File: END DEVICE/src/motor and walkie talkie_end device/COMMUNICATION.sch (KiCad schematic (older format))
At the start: 20 parts, among them IC1 LM4871, J3 speaker_conn, U2 Ai-Thinker-Ra-02, U3 SA818-1W, U4 LP_Filter, U5 MCP41010

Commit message: third commit:very minor changes
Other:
- moved on the sheet: C9, U2
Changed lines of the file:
@@
 Wire Wire Line
 	8300 2050 8300 1850
-Text GLabel 2000 6150 0    50   Input ~ 0
+Text GLabel 3800 6150 0    50   Input ~ 0
 MOSI
-Text GLabel 2000 6050 0    50   Input ~ 0
+Text GLabel 3800 6050 0    50   Input ~ 0
 MISO
-Text GLabel 2000 5950 0    50   Input ~ 0
+Text GLabel 3800 5950 0    50   Input ~ 0
 SCK
 $Comp
 L power:+3.3V #PWR0136
 U 1 1 614532C2
-P 2700 4950
-F 0 "#PWR0136" H 2700 4800 50  0001 C CNN
-F 1 "+3.3V" H 2715 5123 50  0000 C CNN
-F 2 "" H 2700 4950 50  0001 C CNN
-F 3 "" H 2700 4950 50  0001 C CNN
-	1    2700 4950
+P 4500 4950
+F 0 "#PWR0136" H 4500 4800 50  0001 C CNN
+F 1 "+3.3V" H 4515 5123 50  0000 C CNN
+F 2 "" H 4500 4950 50  0001 C CNN
+F 3 "" H 4500 4950 50  0001 C CNN
+	1    4500 4950
 	1    0    0    -1
 $EndComp
 Wire Wire Line
-	2200 6150 2000 6150
+	4000 6150 3800 6150
 Wire Wire Line
-	2000 6050 2200 6050
+	3800 6050 4000 6050
 Wire Wire Line
-	2200 5950 2000 5950
+	4000 5950 3800 5950
 Wire Wire Line
-	2000 5850 2200 5850
+	3800 5850 4000 5850
 Wire Wire Line
-	2200 5650 2000 5650
+	4000 5650 3800 5650
 $Comp
 L Device:C_Small C?
 U 1 1 614532CD
-P 3600 5050
+P 5400 5050
 AR Path="/614532CD" Ref="C?"  Part="1"
 AR Path="/6131B829/614532CD" Ref="C9"  Part="1"
-F 0 "C9" V 3829 5050 50  0000 C CNN
-F 1 "100nF" V 3738 5050 50  0000 C CNN
-F 2 "" H 3600 5050 50  0001 C CNN
-F 3 "~" H 3600 5050 50  0001 C CNN
-	1    3600 5050
+F 0 "C9" V 5629 5050 50  0000 C CNN
+F 1 "100nF" V 5538 5050 50  0000 C CNN
+F 2 "" H 5400 5050 50  0001 C CNN
+F 3 "~" H 5400 5050 50  0001 C CNN
+	1    5400 5050
 	-1   0    0    1
 $EndComp
@@
 L remote_devices:Ai-Thinker-Ra-02 U?
 U 1 1 614532D3
-P 2700 5950
+P 4500 5950
 AR Path="/614532D3" Ref="U?"  Part="1"
 AR Path="/6131B829/614532D3" Ref="U2"  Part="1"
-F 0 "U2" H 2250 6700 50  0000 C CNN
-F 1 "Ai-Thinker-Ra-02" H 2250 6600 50  0000 C CNN
-F 2 "Remote_devices:Ai-Thinker-Ra-02-LoRa" H 3700 5550 50  0001 C CNN
-F 3 "https://mikroelectron.com/Product/10KM-433M-LORA-LONG-RANGE-WIRELESS-MODULE-RA-01" H 2800 6650 50  0001 C CNN
-	1    2700 5950
+F 0 "U2" H 4050 6700 50  0000 C CNN
+F 1 "Ai-Thinker-Ra-02" H 4050 6600 50  0000 C CNN
+F 2 "Remote_devices:Ai-Thinker-Ra-02-LoRa" H 5500 5550 50  0001 C CNN
+F 3 "https://mikroelectron.com/Product/10KM-433M-LORA-LONG-RANGE-WIRELESS-MODULE-RA-01" H 4600 6650 50  0001 C CNN
+	1    4500 5950
 	1    0    0    -1
 $EndComp
 Wire Wire Line
-	3600 4900 3600 4950
+	5400 4900 5400 4950
 $Comp
 L power:GND #PWR0137
 U 1 1 614532DA
-P 3600 5200
-F 0 "#PWR0137" H 3600 4950 50  0001 C CNN
-F 1 "GND" H 3605 5027 50  0000 C CNN
-F 2 "" H 3600 5200 50  0001 C CNN
-F 3 "" H 3600 5200 50  0001 C CNN
-	1    3600 5200
+P 5400 5200
+F 0 "#PWR0137" H 5400 4950 50  0001 C CNN
+F 1 "GND" H 5405 5027 50  0000 C CNN
+F 2 "" H 5400 5200 50  0001 C CNN
+F 3 "" H 5400 5200 50  0001 C CNN
+	1    5400 5200
 	1    0    0    -1
 $EndComp
@@
 L power:GND #PWR0138
 U 1 1 614532E0
-P 2700 6800
-F 0 "#PWR0138" H 2700 6550 50  0001 C CNN
-F 1 "GND" H 2705 6627 50  0000 C CNN
-F 2 "" H 2700 6800 50  0001 C CNN
-F 3 "" H 2700 6800 50  0001 C CNN
-	1    2700 6800
+P 4500 6800
+F 0 "#PWR0138" H 4500 6550 50  0001 C CNN
+F 1 "GND" H 4505 6627 50  0000 C CNN
+F 2 "" H 4500 6800 50  0001 C CNN
+F 3 "" H 4500 6800 50  0001 C CNN
+	1    4500 6800
 	1    0    0    -1
 $EndComp
 Wire Wire Line
-	2700 6800 2700 6750
+	4500 6800 4500 6750
 Wire Wire Line
-	2600 6650 2600 6750
+	4400 6650 4400 6750
 Wire Wire Line
-	2600 6750 2700 6750
+	4400 6750 4500 6750
 Wire Wire Line
-	2800 6650 2800 6750
+	4600 6650 4600 6750
 Wire Wire Line
-	2800 6750 2700 6750
-Connection ~ 2700 6750
-Text GLabel 3400 5550 2    50   Input ~ 0
+	4600 6750 4500 6750
+Connection ~ 4500 6750
+Text GLabel 5200 5550 2    50   Input ~ 0
 DIO0
 Wire Wire Line
-	2700 4950 2700 5050
+	4500 4950 4500 5050
 Wire Wire Line
-	3600 5200 3600 5150
+	5400 5200 5400 5150
 Wire Wire Line
-	3600 4900 3100 4900
+	5400 4900 4900 4900
 Wire Wire Line
-	3100 4900 3100 5050
+	4900 4900 4900 5050
 Wire Wire Line
-	3100 5050 2700 5050
-Connection ~ 2700 5050
+	4900 5050 4500 5050
+Connection ~ 4500 5050
 Wire Wire Line
-	2700 5050 2700 5150
-Text GLabel 3400 5650 2    50   Input ~ 0
+	4500 5050 4500 5150
+Text GLabel 5200 5650 2    50   Input ~ 0
 DIO1
-Text GLabel 3400 5750 2    50   Input ~ 0
+Text GLabel 5200 5750 2    50   Input ~ 0
 DIO2
 Wire Wire Line
-	3200 5550 3400 5550
+	5000 5550 5200 5550
 Wire Wire Line
-	3400 5650 3200 5650
+	5200 5650 5000 5650
 Wire Wire Line
-	3200 5750 3400 5750
-NoConn ~ 3200 5850
-NoConn ~ 3200 5950
-NoConn ~ 3200 6050
-Text Notes 1050 4650 0    50   ~ 10
+	5000 5750 5200 5750
+NoConn ~ 5000 5850
+NoConn ~ 5000 5950
+NoConn ~ 5000 6050
+Text Notes 2850 4650 0    50   ~ 10
 RA-02 LORA MODULE
 Wire Notes Line
-	4700 4400 4700 7700
+	6500 4400 6500 7700
 Wire Notes Line
-	4700 7700 600  7700
+	6500 7700 2400 7700
 Wire Notes Line
-	600  7700 600  4400
+	2400 7700 2400 4400
 Wire Notes Line
 	10850 2500 10850 2750
@@
 Text Notes 6150 3300 0    50   ~ 0
 Digital Potentiometer uses \nSPI protocol to change resistance\nused for setting the volume of the speaker
-Text GLabel 2000 5850 0    50   Input ~ 0
+Text GLabel 3800 5850 0    50   Input ~ 0
 lora_SS
 Text GLabel 5600 2300 0    50   Input ~ 0
@@
 Wire Notes Line
 	1150 2650 1200 2650
-Text GLabel 2000 5650 0    50   Input ~ 0
+Text GLabel 3800 5650 0    50   Input ~ 0
 RST
 Wire Notes Line
-	600  4400 4700 4400
+	2400 4400 6500 4400
 Wire Notes Line
 	4700 4250 600  4250

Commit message: commit 4:minor changes
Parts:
- U: renamed from U2; footprint Remote_devices:Ai-Thinker-Ra-02-LoRa -> RF_Module:Ai-Thinker-Ra-01-LoRa
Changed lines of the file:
@@
 P 4500 5950
 AR Path="/614532D3" Ref="U?"  Part="1"
-AR Path="/6131B829/614532D3" Ref="U2"  Part="1"
-F 0 "U2" H 4050 6700 50  0000 C CNN
+AR Path="/6131B829/614532D3" Ref="U"  Part="1"
+F 0 "U" H 4050 6700 50  0000 C CNN
 F 1 "Ai-Thinker-Ra-02" H 4050 6600 50  0000 C CNN
-F 2 "Remote_devices:Ai-Thinker-Ra-02-LoRa" H 5500 5550 50  0001 C CNN
+F 2 "RF_Module:Ai-Thinker-Ra-01-LoRa" H 5500 5550 50  0001 C CNN
 F 3 "https://mikroelectron.com/Product/10KM-433M-LORA-LONG-RANGE-WIRELESS-MODULE-RA-01" H 4600 6650 50  0001 C CNN
 	1    4500 5950
@@
 Wire Wire Line
 	5400 4900 5400 4950
-$Comp
-L power:GND #PWR0137
-U 1 1 614532DA
-P 5400 5200
-F 0 "#PWR0137" H 5400 4950 50  0001 C CNN
-F 1 "GND" H 5405 5027 50  0000 C CNN
-F 2 "" H 5400 5200 50  0001 C CNN
-F 3 "" H 5400 5200 50  0001 C CNN
-	1    5400 5200
-	1    0    0    -1
-$EndComp
 $Comp
 L power:GND #PWR0138
@@
 Wire Wire Line
 	4500 6800 4500 6750
-Wire Wire Line
-	4400 6650 4400 6750
 Wire Wire Line
 	4400 6750 4500 6750
@@
 Wire Notes Line
 	4700 4250 600  4250
+$Comp
+L power:GND #PWR0137
+U 1 1 62395891
+P 5400 5200
+F 0 "#PWR0137" H 5400 4950 50  0001 C CNN
+F 1 "GND" H 5405 5027 50  0000 C CNN
+F 2 "" H 5400 5200 50  0001 C CNN
+F 3 "" H 5400 5200 50  0001 C CNN
+	1    5400 5200
+	1    0    0    -1
+$EndComp
+Wire Wire Line
+	4400 6650 4400 6750
 $EndSCHEMATC

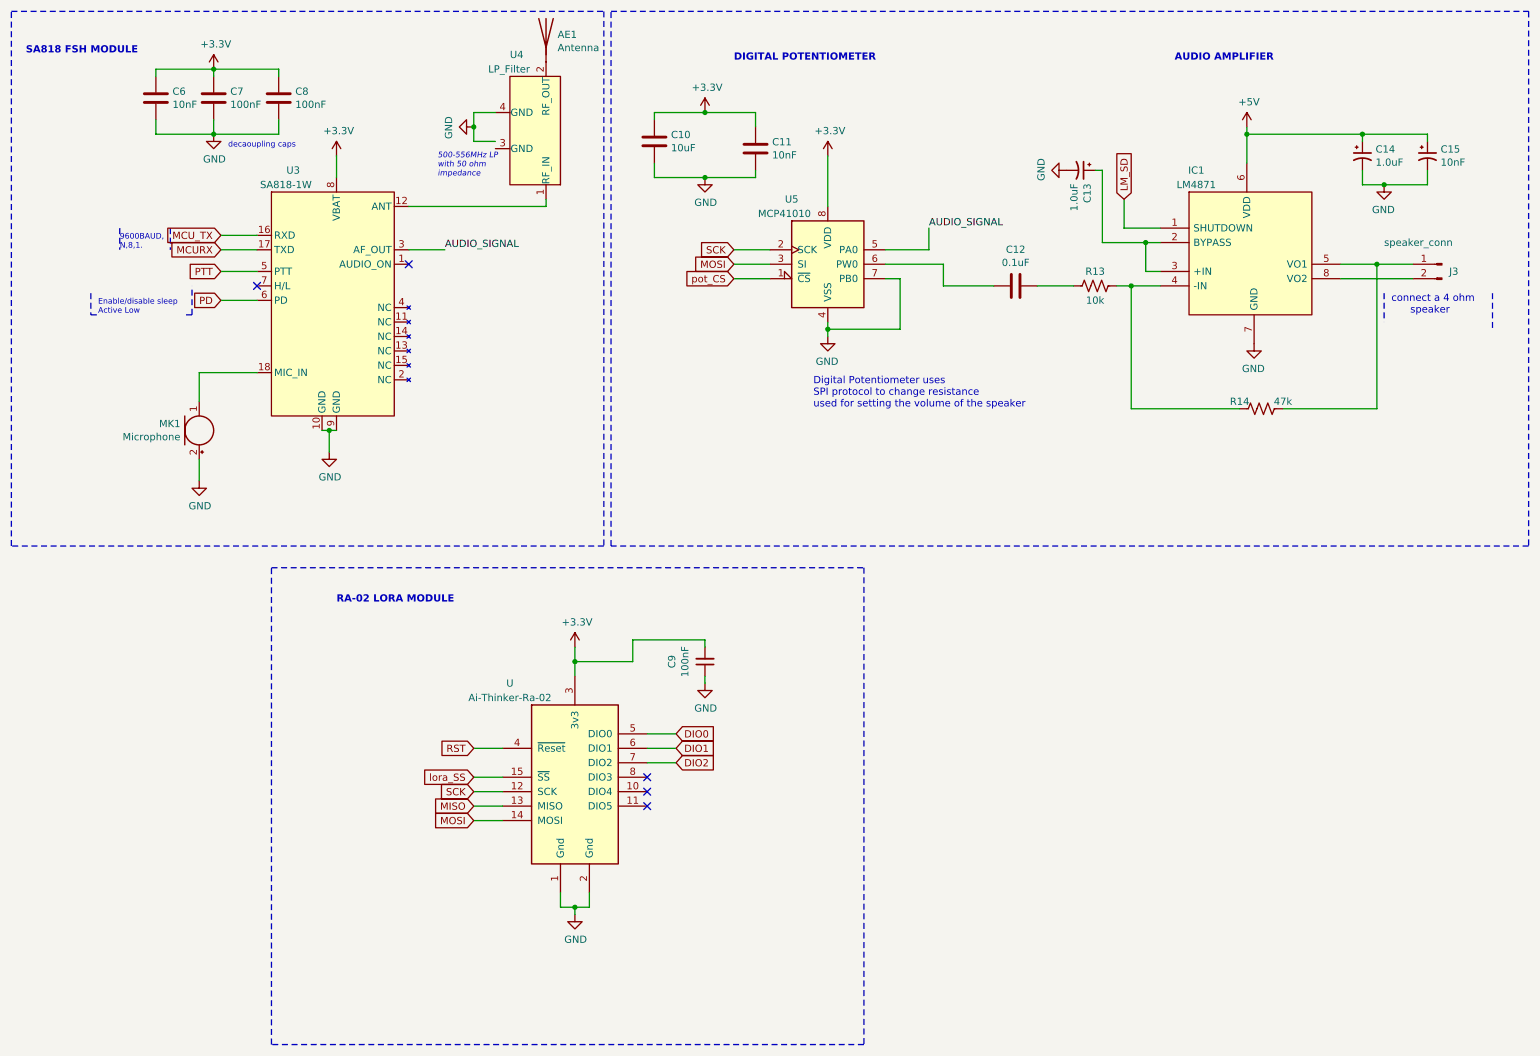
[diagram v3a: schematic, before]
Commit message: All footprint associations updated
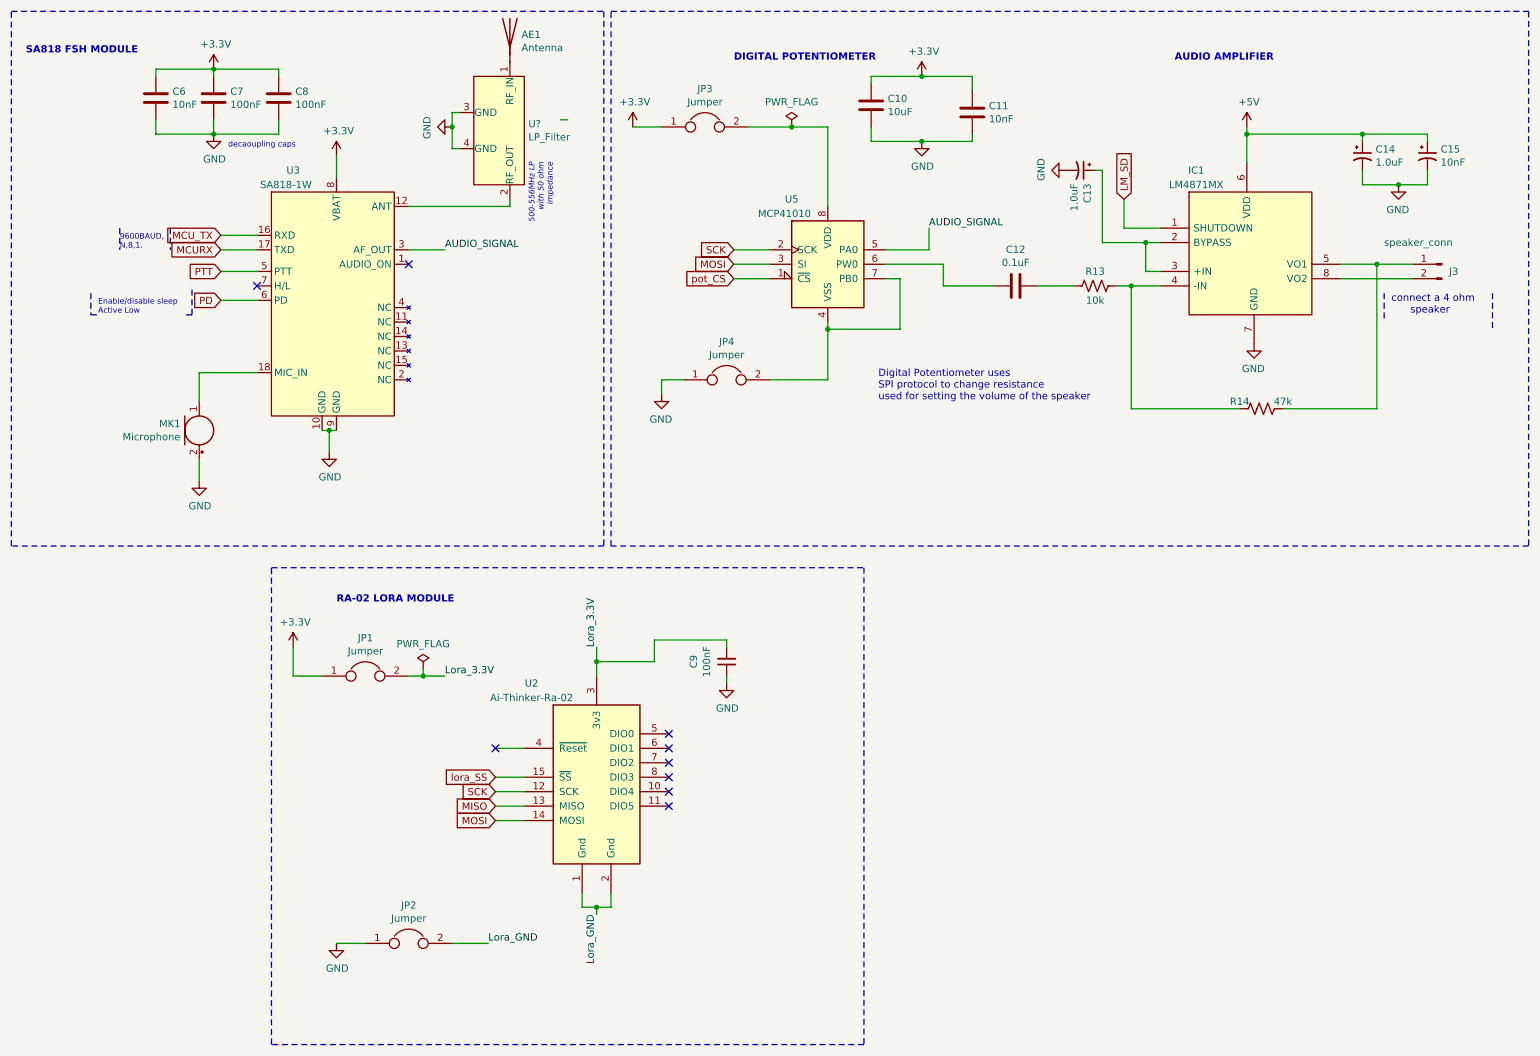
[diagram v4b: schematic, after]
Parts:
- removed U4: LP_Filter, symbol remote_devices:LP_Filter
- added JP1, JP2, JP3, JP4: Jumper, TestPoint:TestPoint_2Pads_Pitch2.54mm_Drill0.8mm, symbol Device:Jumper
- added U?: LP_Filter, symbol remote_devices:LP_Filter
- AE1: footprint (none) -> CoAxial connector:SMA_Amphenol_901-144_Vertical
- C10, C11, C12, C6, C7, C8, C9: footprint (none) -> Capacitor_SMD:C_0603_1608Metric
- C13, C14, C15: footprint (none) -> Capacitor_Tantalum_SMD:CP_EIA-2012-12_Kemet-R
- IC1: value LM4871 -> LM4871MX; footprint SOP65P490X110-8N -> Package_SO:SOP-8_3.9x4.9mm_P1.27mm
- J3: footprint (none) -> Connector_JST:JST_PH_B2B-PH-K_1x02_P2.00mm_Vertical
- MK1: footprint (none) -> Remote_devices:CMEJ974537P
- R13, R14: footprint (none) -> Resistor_SMD:R_0603_1608Metric
- U3: footprint (none) -> Remote_devices:SA818-1W
- U5: footprint (none) -> SamacSys_Parts_2:SOIC127P600X175-8N
- renumbered U to U2
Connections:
- net +3V3: now also JP1.1, JP3.1; no longer C9.2, U2.3 (3v3), U5.8 (VDD)
- net GND: now also JP2.1, JP4.1, U?.3 (GND), U?.4 (GND); no longer U2.1 (Gnd), U2.16 (Gnd), U2.2 (Gnd), U2.9 (Gnd), U5.4 (VSS), U5.7 (PB0)
- net at U3.12 (ANT): now also U?.2 (RF_OUT)
- net at AE1.1 (A): now also U?.1 (RF_IN)
- net DIO0: no longer names the net of U2.5 (DIO0)
- net DIO1: no longer names the net of U2.6 (DIO1)
- net DIO2: no longer names the net of U2.7 (DIO2)
- net RST: no longer names the net of U2.4 (~Reset)
- new net: JP4.2, U5.4 (VSS), U5.7 (PB0)
- new net: JP3.2, U5.8 (VDD)
- new net Lora_3.3V: C9.2, JP1.2, U2.3 (3v3)
- new net Lora_GND: JP2.2, U2.1 (Gnd), U2.16 (Gnd), U2.2 (Gnd), U2.9 (Gnd)
- no-connect marks 5 -> 9
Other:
- moved on the sheet: AE1, C10, C11, C9, U2

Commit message: Project 99% complete and ready:Revision Needed
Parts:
- U4: renamed from U?; footprint (none) -> Remote_devices:LFCN-530
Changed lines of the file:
@@
 	4050 1900 3350 1900
 $Comp
-L remote_devices:LP_Filter U?
+L remote_devices:LP_Filter U4
 U 1 1 627B3A36
 P 4150 1400
-F 0 "U?" V 4079 1428 50  0000 L CNN
+F 0 "U4" V 4079 1428 50  0000 L CNN
 F 1 "LP_Filter" V 4170 1428 50  0000 L CNN
-F 2 "" H 4150 1400 50  0001 C CNN
+F 2 "Remote_devices:LFCN-530" H 4150 1400 50  0001 C CNN
 F 3 "" H 4150 1400 50  0001 C CNN
 	1    4150 1400

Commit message: 90% complete and. PCB done with tracks and design rules verified as well as dimensions
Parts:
- removed C11: 10nF, Capacitor_SMD:C_0603_1608Metric, symbol Device:C
- removed JP3, JP4: Jumper, TestPoint:TestPoint_2Pads_Pitch2.54mm_Drill0.8mm, symbol Device:Jumper
- C14: value 1.0uF -> 1.0uF_TCMIA106AT; Nfr No. (none) -> TCMIA106AT; Supplier (none) -> DIgiKey
- C15: value 10nF -> 1.0uF_TCMIA106AT; Nfr No. (none) -> TCMIA106AT; Supplier (none) -> DIgiKey
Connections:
- net Lora_3.3V: now also U5.8 (VDD)
- net Lora_GND: now also U5.4 (VSS), U5.7 (PB0)
- net MISO: now also U5.3 (SI)
- net MOSI: no longer U5.3 (SI)
- net MCURX renamed MCU_RX
- net lora_SS renamed LORA_SS
- net pot_CS renamed POT_CS
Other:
- moved on the sheet: C10
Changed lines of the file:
@@
 $Descr A4 11693 8268
 encoding utf-8
-Sheet 2 4
+Sheet 4 4
 Title ""
 Date ""
@@
 Wire Wire Line
 	2850 1550 2850 1700
-Text GLabel 2050 2350 0    50   Input ~ 0
-PTT
 Wire Wire Line
 	2300 2350 2050 2350
-Text GLabel 2050 2550 0    50   Input ~ 0
-PD
 Wire Wire Line
 	2300 2550 2050 2550
@@
 Wire Wire Line
 	2050 2200 2300 2200
-Text GLabel 2050 2200 0    50   Input ~ 0
-MCURX
 Wire Wire Line
 	2050 2100 2300 2100
-Text GLabel 2050 2100 0    50   Input ~ 0
-MCU_TX
 NoConn ~ 3350 2300
 NoConn ~ 2300 2450
@@
 L Device:C C10
 U 1 1 61336022
-P 6550 1200
-F 0 "C10" H 6665 1246 50  0000 L CNN
-F 1 "10uF" H 6665 1155 50  0000 L CNN
-F 2 "Capacitor_SMD:C_0603_1608Metric" H 6588 1050 50  0001 C CNN
-F 3 "~" H 6550 1200 50  0001 C CNN
-	1    6550 1200
-	1    0    0    -1
-$EndComp
-$Comp
-L Device:C C11
-U 1 1 61336028
-P 7250 1250
-F 0 "C11" H 7365 1296 50  0000 L CNN
-F 1 "10nF" H 7365 1205 50  0000 L CNN
-F 2 "Capacitor_SMD:C_0603_1608Metric" H 7288 1100 50  0001 C CNN
-F 3 "~" H 7250 1250 50  0001 C CNN
-	1    7250 1250
-	1    0    0    -1
-$EndComp
-Wire Wire Line
-	6550 1050 6550 1000
-Wire Wire Line
-	6550 1000 6900 1000
-Connection ~ 6900 1000
+P 6900 1200
+F 0 "C10" H 7015 1246 50  0000 L CNN
+F 1 "10uF" H 7015 1155 50  0000 L CNN
+F 2 "Capacitor_SMD:C_0603_1608Metric" H 6938 1050 50  0001 C CNN
+F 3 "~" H 6900 1200 50  0001 C CNN
+	1    6900 1200
+	1    0    0    -1
+$EndComp
+Wire Wire Line
+	6900 1050 6900 1000
 $Comp
 L power:+3.3V #PWR0126
@@
 	1    0    0    -1
 $EndComp
-Connection ~ 6900 1450
-Wire Wire Line
-	6900 1450 7250 1450
-Wire Wire Line
-	6550 1450 6900 1450
-Wire Wire Line
-	7250 1000 7250 1100
-Wire Wire Line
-	7250 1400 7250 1450
-Wire Wire Line
-	6900 1000 7250 1000
-Wire Wire Line
-	6550 1350 6550 1450
+Wire Wire Line
+	6900 1350 6900 1450
 Wire Wire Line
 	5600 2200 5850 2200
@@
 Text Label 6950 2050 0    50   ~ 0
 AUDIO_SIGNAL
-$Comp
-L power:GND #PWR0128
-U 1 1 6133604C
-P 5100 3200
-F 0 "#PWR0128" H 5100 2950 50  0001 C CNN
-F 1 "GND" H 5105 3027 50  0000 C CNN
-F 2 "" H 5100 3200 50  0001 C CNN
-F 3 "" H 5100 3200 50  0001 C CNN
-	1    5100 3200
-	-1   0    0    -1
-$EndComp
-$Comp
-L power:+3.3V #PWR0129
-U 1 1 61336053
-P 4900 1350
-F 0 "#PWR0129" H 4900 1200 50  0001 C CNN
-F 1 "+3.3V" H 4915 1523 50  0000 C CNN
-F 2 "" H 4900 1350 50  0001 C CNN
-F 3 "" H 4900 1350 50  0001 C CNN
-	1    4900 1350
-	1    0    0    -1
-$EndComp
 $Comp
 L Potentiometer_Digital:MCP41010 U5
@@
 P 9950 1550
 F 0 "C14" H 10041 1596 50  0000 L CNN
-F 1 "1.0uF" H 10041 1505 50  0000 L CNN
+F 1 "1.0uF_TCMIA106AT" H 9600 1450 50  0000 L CNN
 F 2 "Capacitor_Tantalum_SMD:CP_EIA-2012-12_Kemet-R" H 9950 1550 50  0001 C CNN
 F 3 "~" H 9950 1550 50  0001 C CNN
+F 4 "TCMIA106AT" H 9950 1550 50  0001 C CNN "Nfr No."
+F 5 "DIgiKey" H 9950 1550 50  0001 C CNN "Supplier"
 	1    9950 1550
 	1    0    0    -1
@@
 Wire Wire Line
 	8450 2150 8150 2150
-Text GLabel 8300 1850 1    50   Input ~ 0
-LM_SD
 Wire Wire Line
 	8150 2150 8150 1650
 Wire Wire Line
 	8150 1650 8100 1650
-$Comp
-L Device:CP1_Small C15
-U 1 1 613360FF
-P 10400 1550
-F 0 "C15" H 10491 1596 50  0000 L CNN
-F 1 "10nF" H 10491 1505 50  0000 L CNN
-F 2 "Capacitor_Tantalum_SMD:CP_EIA-2012-12_Kemet-R" H 10400 1550 50  0001 C CNN
-F 3 "~" H 10400 1550 50  0001 C CNN
-	1    10400 1550
-	1    0    0    -1
-$EndComp
 Wire Wire Line
 	10400 1650 10400 1750
@@
 Wire Wire Line
 	8550 2050 8300 2050
-Wire Wire Line
-	8300 2050 8300 1850
-Text GLabel 3950 6150 0    50   Input ~ 0
-MOSI
-Text GLabel 3950 6050 0    50   Input ~ 0
-MISO
-Text GLabel 3950 5950 0    50   Input ~ 0
-SCK
 $Comp
 L power:+3.3V #PWR0136
@@
 Text Notes 6600 3250 0    50   ~ 0
 Digital Potentiometer uses \nSPI protocol to change resistance\nused for setting the volume of the speaker
-Text GLabel 3950 5850 0    50   Input ~ 0
-lora_SS
-Text GLabel 5600 2300 0    50   Input ~ 0
-MOSI
-Text GLabel 5600 2200 0    50   Input ~ 0
-SCK
-Text GLabel 5600 2400 0    50   Input ~ 0
-pot_CS
 Wire Wire Line
 	5600 2400 5850 2400
@@
 Text Label 4650 6800 3    50   ~ 0
 Lora_GND
-$Comp
-L Device:Jumper JP3
-U 1 1 624157EB
-P 5400 1350
-F 0 "JP3" H 5400 1614 50  0000 C CNN
-F 1 "Jumper" H 5400 1523 50  0000 C CNN
-F 2 "TestPoint:TestPoint_2Pads_Pitch2.54mm_Drill0.8mm" H 5400 1350 50  0001 C CNN
-F 3 "~" H 5400 1350 50  0001 C CNN
-	1    5400 1350
-	1    0    0    -1
-$EndComp
-Wire Wire Line
-	4900 1350 5100 1350
-$Comp
-L Device:Jumper JP4
-U 1 1 6241CC63
-P 5550 3100
-F 0 "JP4" H 5550 3364 50  0000 C CNN
-F 1 "Jumper" H 5550 3273 50  0000 C CNN
-F 2 "TestPoint:TestPoint_2Pads_Pitch2.54mm_Drill0.8mm" H 5550 3100 50  0001 C CNN
-F 3 "~" H 5550 3100 50  0001 C CNN
-	1    5550 3100
-	1    0    0    -1
-$EndComp
-Wire Wire Line
-	5250 3100 5100 3100
-Wire Wire Line
-	5100 3100 5100 3200
 Wire Wire Line
 	5850 3100 6250 3100
@@
 Wire Wire Line
 	3650 1350 3650 1500
+Text HLabel 2050 2100 0    39   Input ~ 0
+MCU_TX
+Text HLabel 2050 2200 0    39   Input ~ 0
+MCU_RX
+Text HLabel 2050 2350 0    39   Input ~ 0
+PTT
+Text HLabel 2050 2550 0    39   Input ~ 0
+PD
+Text HLabel 3950 5850 0    39   Input ~ 0
+LORA_SS
+Text HLabel 3950 5950 0    39   Input ~ 0
+SCK
+Text HLabel 3950 6050 0    39   Input ~ 0
+MISO
+Text HLabel 3950 6150 0    39   Input ~ 0
+MOSI
+Text HLabel 5600 2200 0    39   Input ~ 0
+SCK
+Text HLabel 5600 2300 0    39   Input ~ 0
+MISO
+Text HLabel 5600 2400 0    39   Input ~ 0
+POT_CS
+Text HLabel 8300 1750 1    39   Input ~ 0
+LM_SD
+Wire Wire Line
+	8300 1750 8300 2050
+Text Label 5850 3100 2    50   ~ 0
+Lora_GND
+Text Label 5700 1350 2    50   ~ 0
+Lora_3.3V
+$Comp
+L Device:CP1_Small C15
+U 1 1 615CD3DF
+P 10400 1550
+F 0 "C15" H 10491 1596 50  0000 L CNN
+F 1 "1.0uF_TCMIA106AT" H 10200 1750 50  0000 L CNN
+F 2 "Capacitor_Tantalum_SMD:CP_EIA-2012-12_Kemet-R" H 10400 1550 50  0001 C CNN
+F 3 "~" H 10400 1550 50  0001 C CNN
+F 4 "TCMIA106AT" H 10400 1550 50  0001 C CNN "Nfr No."
+F 5 "DIgiKey" H 10400 1550 50  0001 C CNN "Supplier"
+	1    10400 1550
+	1    0    0    -1
+$EndComp
 $EndSCHEMATC
